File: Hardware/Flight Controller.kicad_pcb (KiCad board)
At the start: 6 copper layers, 40.6 x 40.5 mm, 166 parts, among them J1 USB4110GFA, J10 CAN BUS, J11 CAN BUS, J2 FPV, J3 ST_LINK, J4 GPS, J5 Airspeed sensor, J6 4in1 ESC, J7 RC Receiver, J8 VTX, J9 DJI, Q1 AO3407A, SW1 reset, SW2 MCU_BOOT, U1 TPS54302, U10 BMI270, U12 BMP388, U13 AT7456E, U14 SN65HVD230, U2 USBLC6-2SC6, U4 AP63205WU, U5 AP2112K-3.3, U6 AP7343-33W5-7, U7 STM32H743VITx, U8 ICM-42688-P, U9 W25Q128JVSIQ, Y1 ASE-8.000MHZ-LC-T, Y2 27Mhz 20pF

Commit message: minor Updates
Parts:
- added R31: 4.7k, Resistor_SMD:R_0402_1005Metric, F.Cu at (141.2, 86.6)
- added R32: 4.7k, Resistor_SMD:R_0402_1005Metric, F.Cu at (140.1, 86.6)
- C19: value 1uF -> 4,7uF
- R29, R30: value 10k -> 7.5k
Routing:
- net GPS_SDA: track 21.5 -> 30.4 mm
- net GPS_SCL: track 22.1 -> 29.6 mm
- net +3.3V: track 108.5 -> 112.9 mm

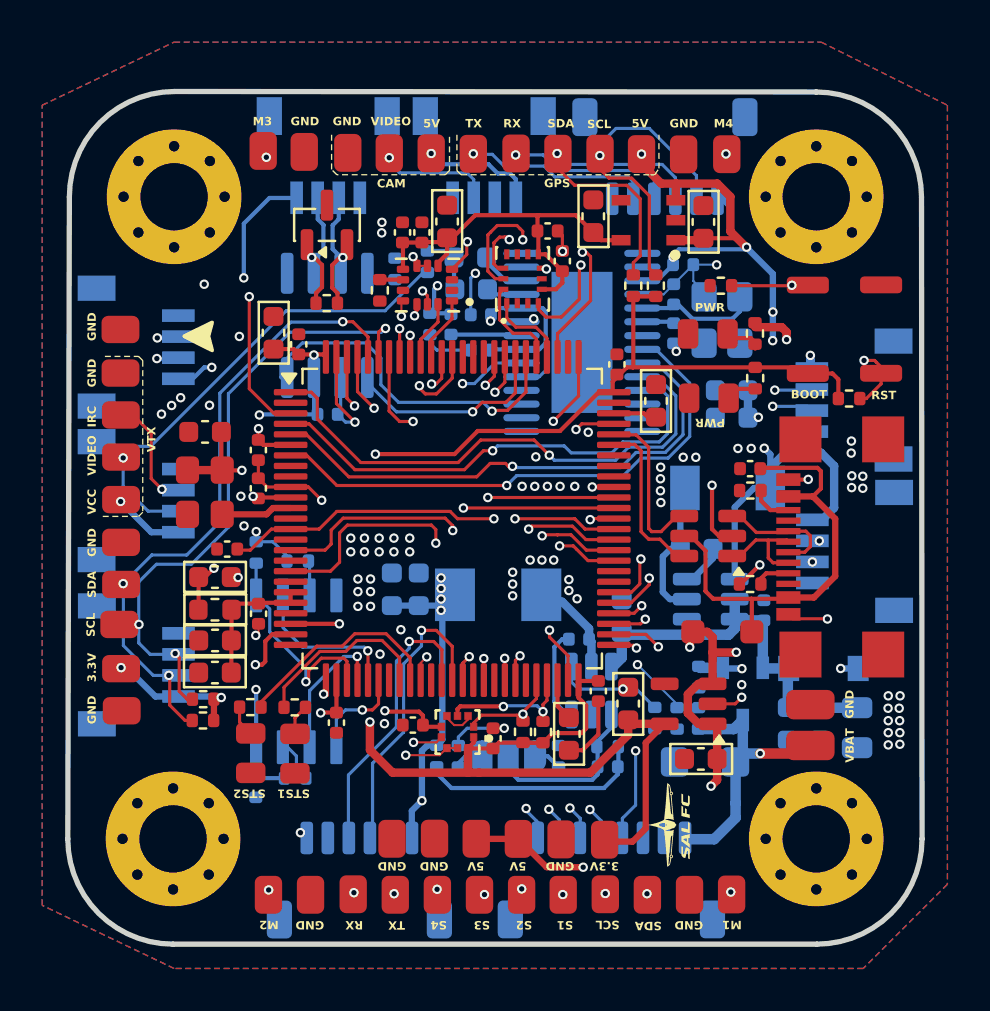
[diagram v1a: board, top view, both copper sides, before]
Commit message: /Hardware : add ground vias to enhance SI and possible emission behaviour
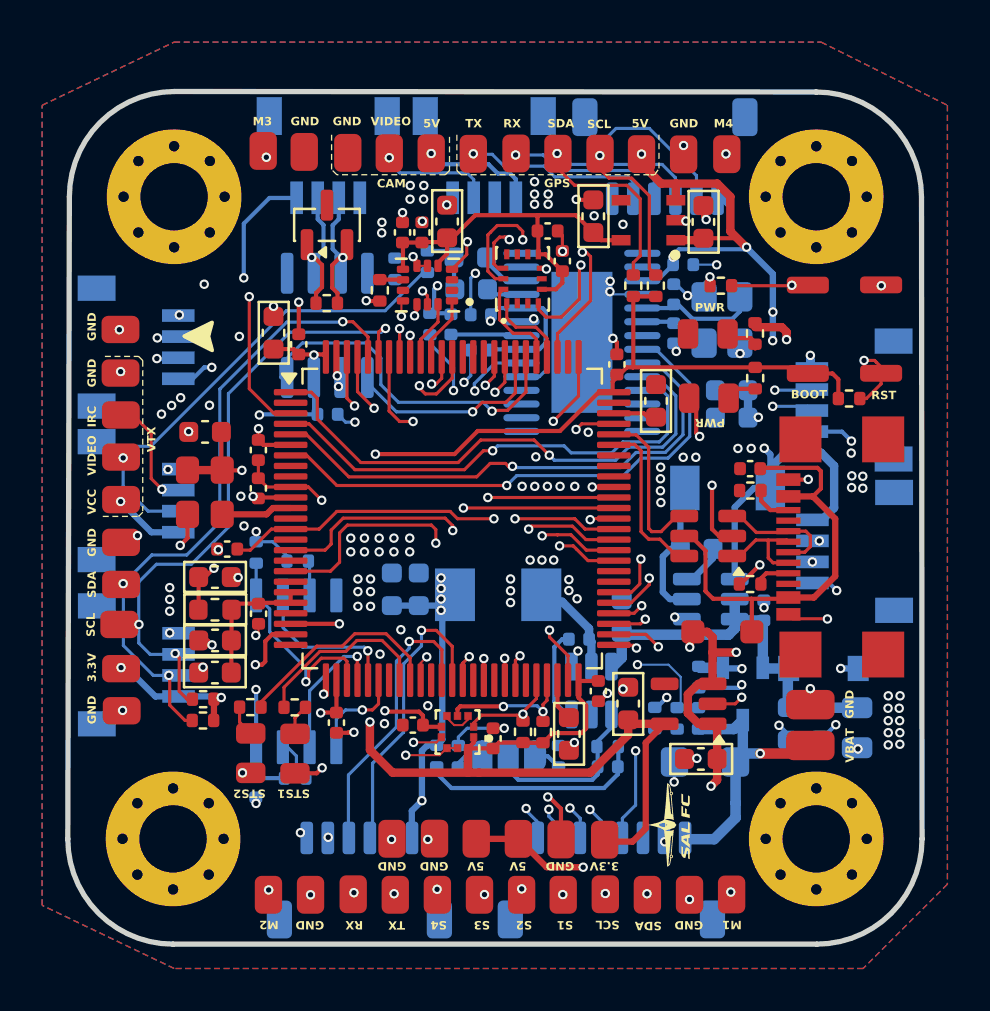
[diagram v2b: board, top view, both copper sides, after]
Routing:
- net GND: track 59.5 -> 82.1 mm, vias 89 -> 162
- net Net-(U7-PC1): track 25.4 -> 26.4 mm

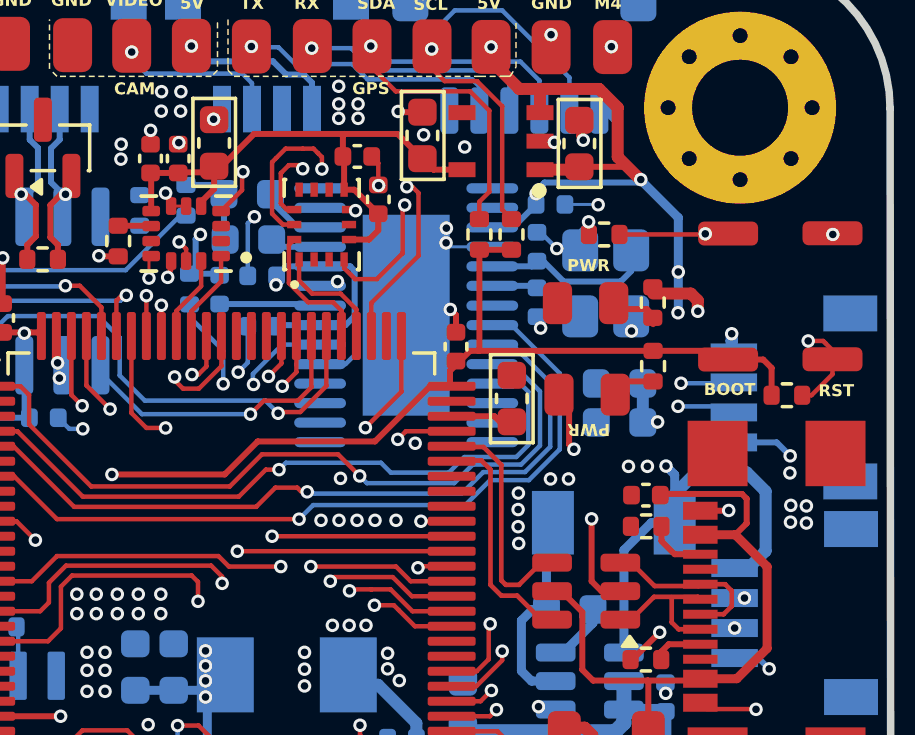
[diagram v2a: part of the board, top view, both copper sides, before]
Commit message: /HARDWARE: Updated BOM do not Include list
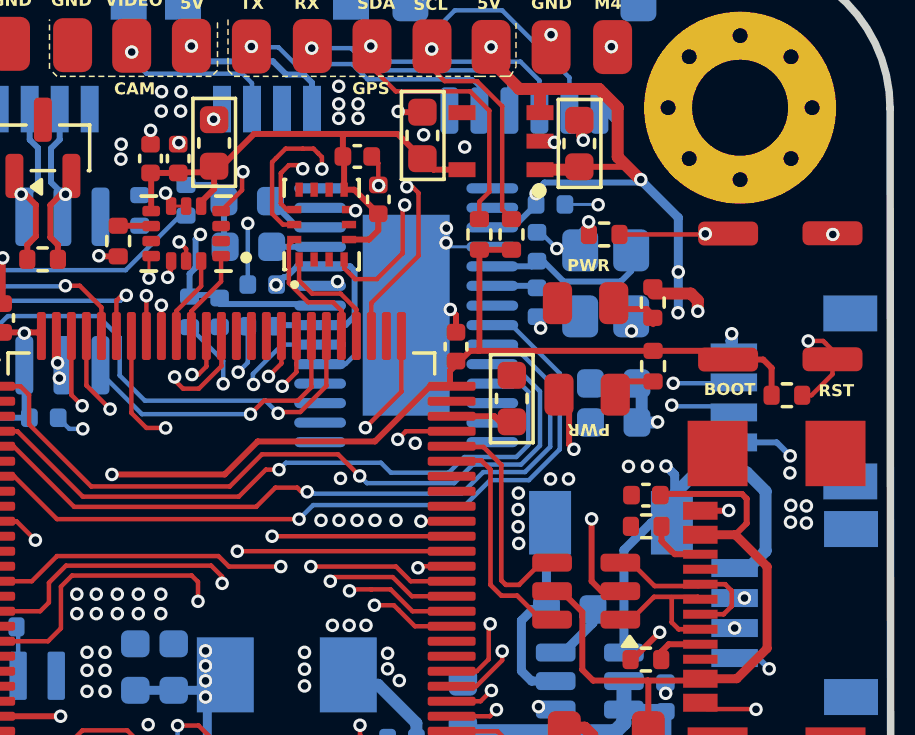
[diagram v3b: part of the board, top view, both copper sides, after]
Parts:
- moved C51 0.76 mm to (131.4, 89.2)
- moved R25 0.76 mm to (130.4, 89.2)
- moved C52 0.29 mm to (132.8, 88.2)
- moved C49 0.24 mm to (132.4, 87.0)
- moved C48 0.23 mm to (132.3, 85.5)
- moved C15 0.19 mm to (144.6, 91.5)
- moved C16 0.19 mm to (144.6, 92.8)
- moved L2 0.09 mm to (144.5, 96.2)
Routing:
- net GND: track 82.1 -> 81.3 mm
- net VIDEO_IN: track 15.1 -> 15.8 mm
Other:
- board text added: "C_H"
- board text added: "C_L"
- board text removed: "+5V"
- board text removed: "CAN_H"
- board text removed: "CAN_L"

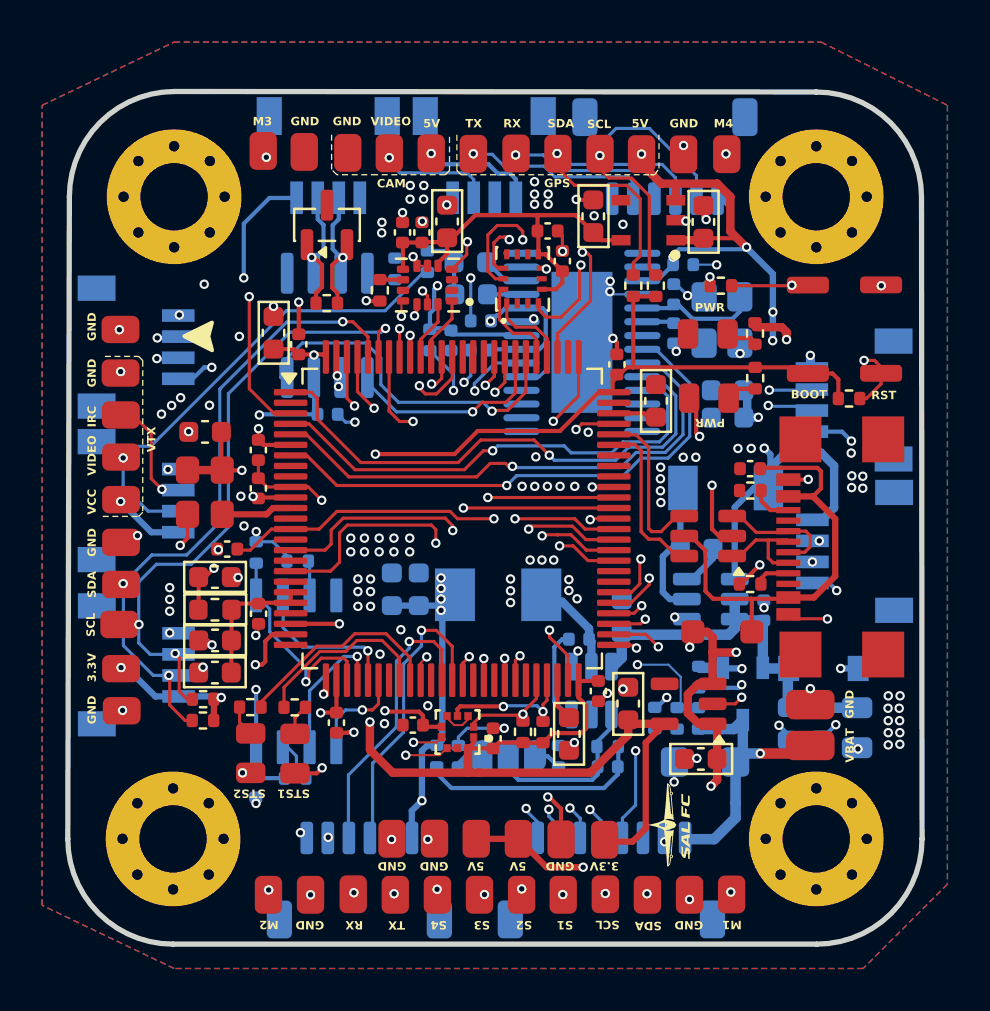
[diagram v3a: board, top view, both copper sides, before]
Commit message: /HARDWARE : Ficed Silkscreen
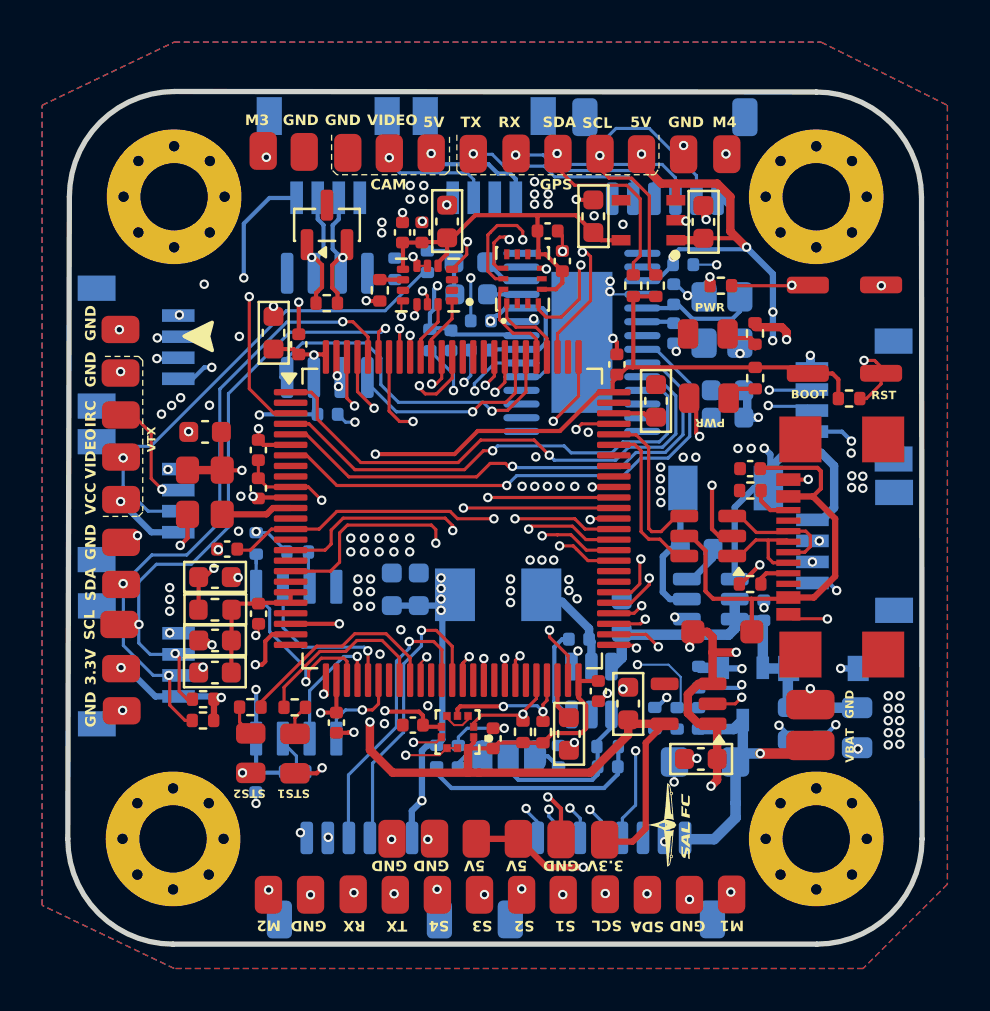
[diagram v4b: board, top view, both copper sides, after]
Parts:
- moved R20 0.43 mm to (124.1, 99.2)
- moved R22 0.43 mm to (122.2, 98.8)
- moved U9 0.41 mm to (124.1, 104.5)
- moved R21 0.30 mm to (124.0, 109.7)
- moved C37 0.25 mm to (122.2, 110.1)
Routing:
- net FLASH_CS: track 10.2 -> 11.1 mm
- net +3.3V: track 112.9 -> 112.2 mm

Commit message: /HARDWARE: Tuned DRC and Board Cleanup
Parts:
- moved G*** 0.56 mm to (127.2, 96.4)
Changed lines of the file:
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@@
 	(footprint "LOGO"
 		(layer "B.Cu")
-		(at 126.64686 96.409699 180)
+		(at 127.205098 96.409699 180)
 		(property "Reference" "G***"
 			(at 0 0 0)
@@
 	(gr_text "TX"
 		(at 147.69 91.85 0)
-		(layer "B.SilkS" knockout)
+		(layer "B.SilkS")
 		(effects
 			(font
@@
 	(gr_text "5V"
 		(at 147.72 90.8 0)
-		(layer "B.SilkS" knockout)
+		(layer "B.SilkS")
 		(effects
 			(font
@@
 	(gr_text "GND"
 		(at 147.72 93.77 0)
-		(layer "B.SilkS" knockout)
+		(layer "B.SilkS")
 		(effects
 			(font
@@
 	(gr_text "TX"
 		(at 147.72 99.05 0)
-		(layer "B.SilkS" knockout)
+		(layer "B.SilkS")
 		(effects
 			(font
@@
 	(gr_text "RX"
 		(at 147.73 92.81 0)
-		(layer "B.SilkS" knockout)
+		(layer "B.SilkS")
 		(effects
 			(font
@@
 	(gr_text "5V"
 		(at 147.74 98.01 0)
-		(layer "B.SilkS" knockout)
+		(layer "B.SilkS")
 		(effects
 			(font
@@
 	(gr_text "GND"
 		(at 147.75 101.02 0)
-		(layer "B.SilkS" knockout)
+		(layer "B.SilkS")
 		(effects
 			(font
@@
 	(gr_text "RX"
 		(at 147.76 100.01 0)
-		(layer "B.SilkS" knockout)
+		(layer "B.SilkS")
 		(effects
 			(font
@@
 	(gr_text "3.3V"
 		(at 124.416594 83.236331 90)
-		(layer "B.SilkS" knockout)
+		(layer "B.SilkS")
 		(effects
 			(font
@@
 	(gr_text "C_L"
 		(at 125.39 83.214603 90)
-		(layer "B.SilkS" knockout)
+		(layer "B.SilkS")
 		(effects
 			(font
@@
 	(gr_text "C_H"
 		(at 126.43 83.224603 90)
-		(layer "B.SilkS" knockout)
+		(layer "B.SilkS")
 		(effects
 			(font
@@
 	(gr_text "GND"
 		(at 127.42 83.224603 90)
-		(layer "B.SilkS" knockout)
+		(layer "B.SilkS")
 		(effects
 			(font
@@
 	(gr_text "GND"
 		(at 139.33 83.27 90)
-		(layer "B.SilkS" knockout)
+		(layer "B.SilkS")
 		(effects
 			(font
@@
 	(gr_text "TX"
 		(at 140.36 83.28 90)
-		(layer "B.SilkS" knockout)
+		(layer "B.SilkS")
 		(effects
 			(font
@@
 	(gr_text "RX"
 		(at 141.39 83.235 90)
-		(layer "B.SilkS" knockout)
+		(layer "B.SilkS")
 		(effects
 			(font
@@
 	(gr_text "SDA\n"
 		(at 142.37 83.26 90)
-		(layer "B.SilkS" knockout)
+		(layer "B.SilkS")
 		(effects
 			(font
@@
 	(gr_text "SCL"
 		(at 143.39 83.26 90)
-		(layer "B.SilkS" knockout)
+		(layer "B.SilkS")
 		(effects
 			(font
@@
 	(gr_text "5V"
 		(at 144.42 83.26 90)
-		(layer "B.SilkS" knockout)
+		(layer "B.SilkS")
 		(effects
 			(font
@@
 	(gr_text "GND"
 		(at 119.315 87.715 180)
-		(layer "B.SilkS" knockout)
+		(layer "B.SilkS")
 		(effects
 			(font
@@
 	(gr_text "CLK"
 		(at 119.32 88.7 180)
-		(layer "B.SilkS" knockout)
+		(layer "B.SilkS")
 		(effects
 			(font
@@
 	(gr_text "DIO\n"
 		(at 119.32 89.7 180)
-		(layer "B.SilkS" knockout)
+		(layer "B.SilkS")
 		(effects
 			(font
@@
 	(gr_text "3V3"
 		(at 119.35 90.71 180)
-		(layer "B.SilkS" knockout)
+		(layer "B.SilkS")
 		(effects
 			(font
@@
 	(gr_text "GND"
 		(at 119.36 94.99 180)
-		(layer "B.SilkS" knockout)
+		(layer "B.SilkS")
 		(effects
 			(font
@@
 	(gr_text "IRC"
 		(at 119.38 96 180)
-		(layer "B.SilkS" knockout)
+		(layer "B.SilkS")
 		(effects
 			(font
@@
 	(gr_text "VCC"
 		(at 119.39 98.02 180)
-		(layer "B.SilkS" knockout)
+		(layer "B.SilkS")
 		(effects
 			(font
@@
 	(gr_text "VID_OUT"
 		(at 119.41 97.04 180)
-		(layer "B.SilkS" knockout)
+		(layer "B.SilkS")
 		(effects
 			(font
@@
 	(gr_text "GND"
 		(at 119.5 102.84 180)
-		(layer "B.SilkS" knockout)
+		(layer "B.SilkS")
 		(effects
 			(font
@@
 	(gr_text "SDA"
 		(at 119.51 103.87 180)
-		(layer "B.SilkS" knockout)
+		(layer "B.SilkS")
 		(effects
 			(font
@@
 	(gr_text "SCL"
 		(at 119.51 104.88 180)
-		(layer "B.SilkS" knockout)
+		(layer "B.SilkS")
 		(effects
 			(font
@@
 	(gr_text "3V3"
 		(at 119.52 105.82 180)
-		(layer "B.SilkS" knockout)
+		(layer "B.SilkS")
 		(effects
 			(font
@@
 	(gr_text "SBUS"
 		(at 124.23 111.954413 270)
-		(layer "B.SilkS" knockout)
+		(layer "B.SilkS")
 		(effects
 			(font
@@
 	(gr_text "GND"
 		(at 125.21 111.944413 270)
-		(layer "B.SilkS" knockout)
+		(layer "B.SilkS")
 		(effects
 			(font
@@
 	(gr_text "DJI_RX"
 		(at 126.21 111.974413 270)
-		(layer "B.SilkS" knockout)
+		(layer "B.SilkS")
 		(effects
 			(font
@@
 	(gr_text "DJI_TX"
 		(at 127.25 111.974413 270)
-		(layer "B.SilkS" knockout)
+		(layer "B.SilkS")
 		(effects
 			(font
@@
 	(gr_text "GND"
 		(at 128.21 111.954413 270)
-		(layer "B.SilkS" knockout)
+		(layer "B.SilkS")
 		(effects
 			(font
@@
 	(gr_text "VCC"
 		(at 129.238534 111.910155 270)
-		(layer "B.SilkS" knockout)
+		(layer "B.SilkS")
 		(effects
 			(font
@@
 	(gr_text "M5"
 		(at 135.19 111.98 270)
-		(layer "B.SilkS" knockout)
+		(layer "B.SilkS")
 		(effects
 			(font
@@
 	(gr_text "M6"
 		(at 136.23 111.96 270)
-		(layer "B.SilkS" knockout)
+		(layer "B.SilkS")
 		(effects
 			(font
@@
 	(gr_text "M7"
 		(at 137.23 112 270)
-		(layer "B.SilkS" knockout)
+		(layer "B.SilkS")
 		(effects
 			(font
@@
 	(gr_text "M8"
 		(at 138.23 111.995018 270)
-		(layer "B.SilkS" knockout)
+		(layer "B.SilkS")
 		(effects
 			(font
@@
 	(gr_text "CURR"
 		(at 139.21 112.005018 270)
-		(layer "B.SilkS" knockout)
+		(layer "B.SilkS")
 		(effects
 			(font
@@
 	(gr_text "GND"
 		(at 141.19 111.96 270)
-		(layer "B.SilkS" knockout)
+		(layer "B.SilkS")
 		(effects
 			(font
@@
 	(gr_text "VBAT"
 		(at 142.25 111.94 270)
-		(layer "B.SilkS" knockout)
+		(layer "B.SilkS")
 		(effects
 			(font
@@
 	(gr_text "GND"
 		(at 131.83 83.13 90)
-		(layer "B.SilkS" knockout)
+		(layer "B.SilkS")
 		(effects
 			(font
@@
 	(gr_text "VID"
 		(at 132.83 83.24 90)
-		(layer "B.SilkS" knockout)
+		(layer "B.SilkS")
 		(effects
 			(font
@@
 	(gr_text "5V"
 		(at 134.85 83.19 90)
-		(layer "B.SilkS" knockout)
+		(layer "B.SilkS")
 		(effects
 			(font
